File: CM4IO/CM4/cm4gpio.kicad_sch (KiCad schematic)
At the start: 2 parts

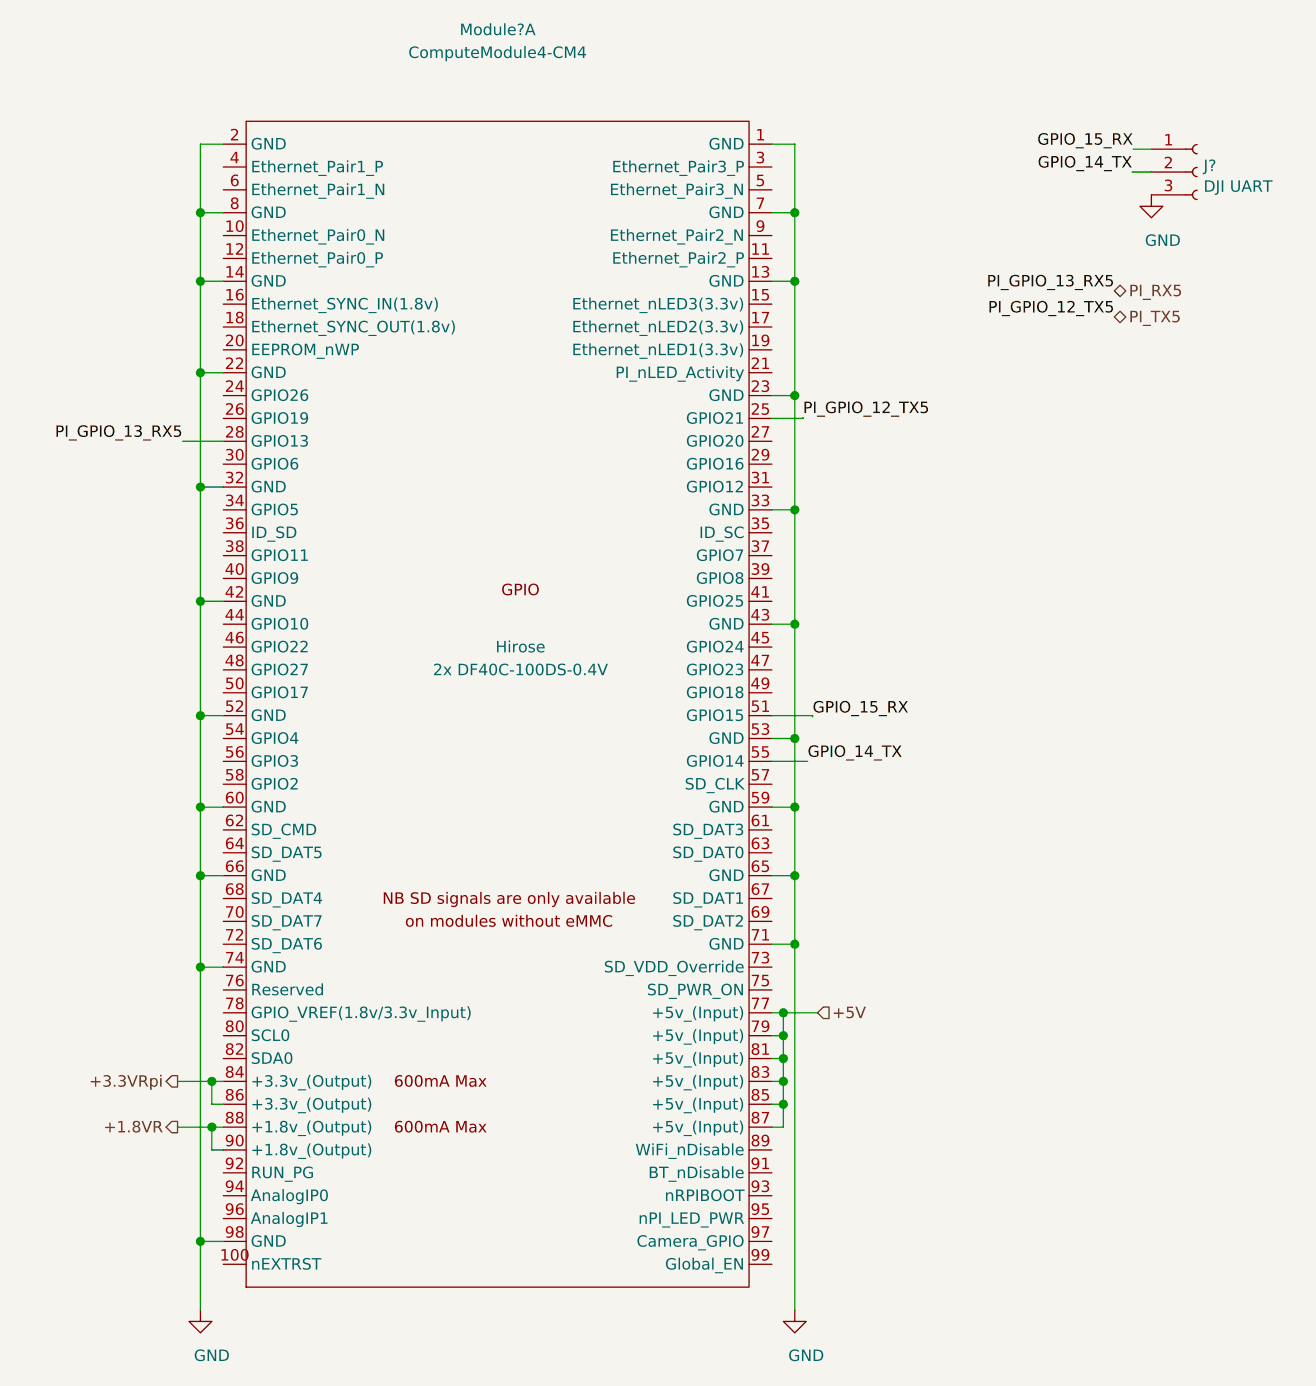
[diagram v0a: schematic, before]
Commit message: Initial CM4IO board design
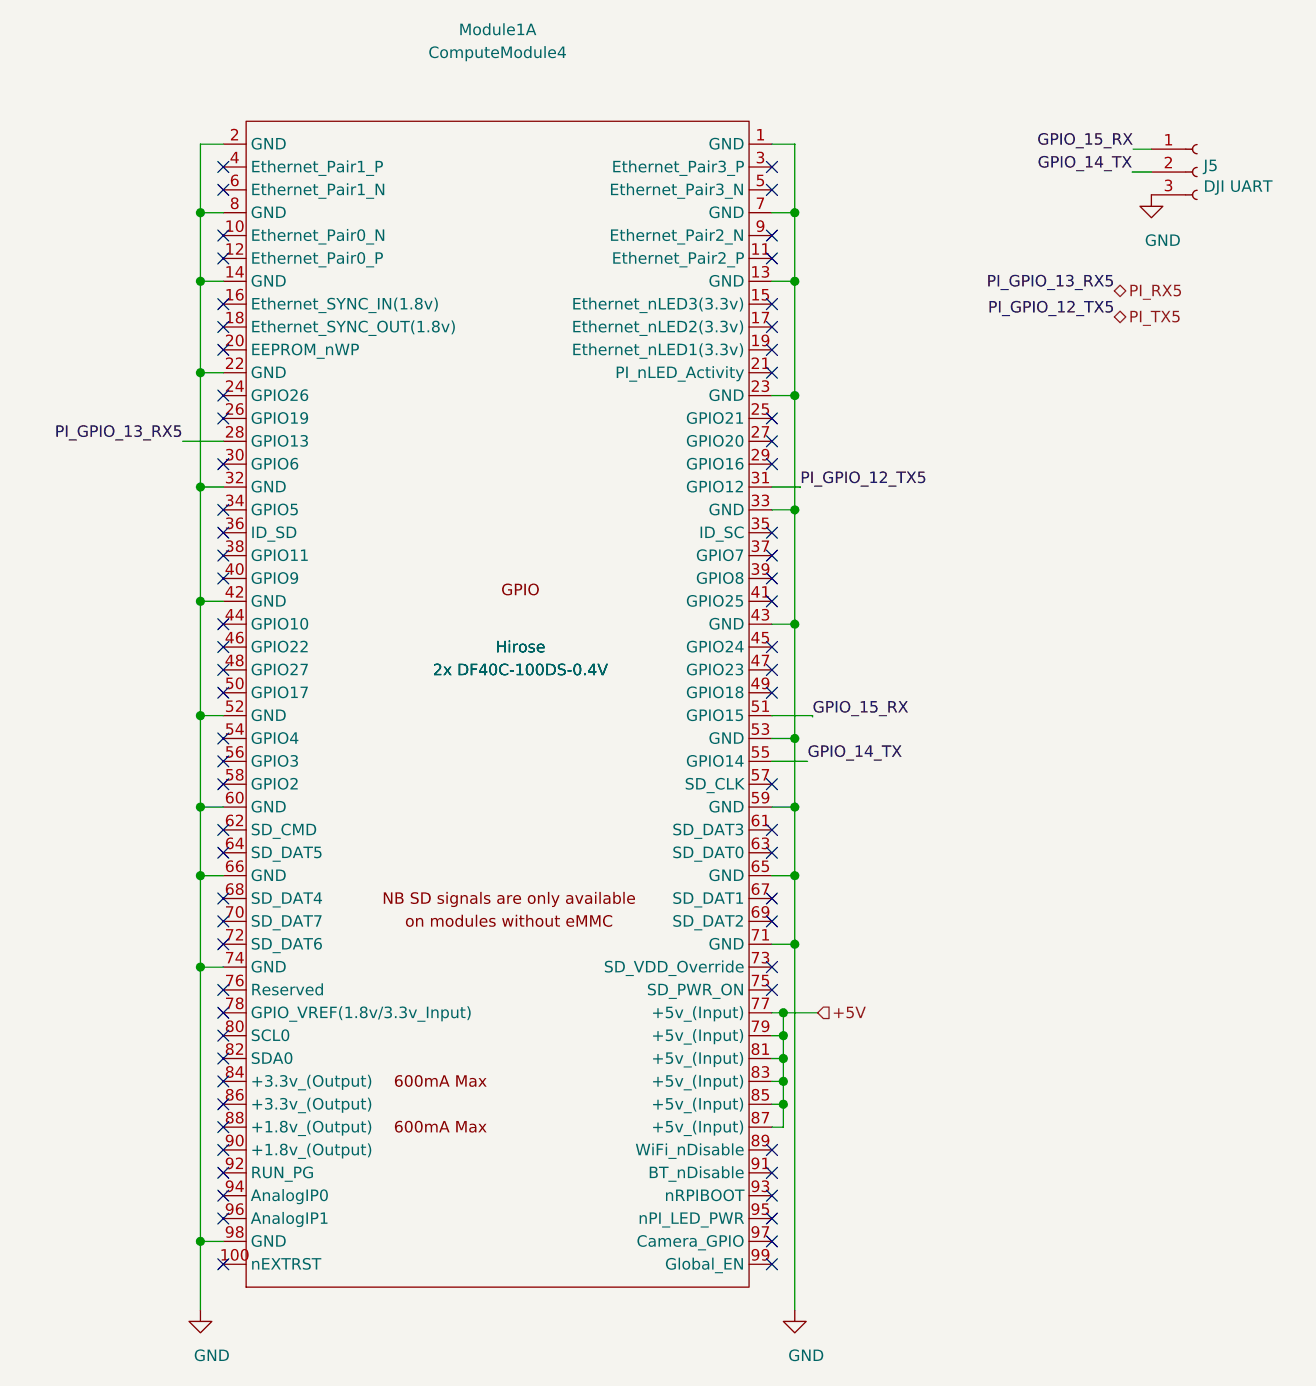
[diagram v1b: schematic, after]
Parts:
- J5: renamed from J?; footprint (none) -> Connector_Molex:Molex_PicoBlade_53261-0371_1x03-1MP_P1.25mm_Horizontal
- Module1: renamed from Module?; value ComputeModule4-CM4 -> ComputeModule4; Field4 (none) -> Hirose; Field5 (none) -> 2x DF40C-100DS-0.4V
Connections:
- net PI_TX5: now also Module1.31 (GPIO12); no longer Module1.25 (GPIO21)
- net +1.8VR: no longer names the net of Module1.88 (+1.8v_(Output))
- net +1.8VR: no longer Module1.90 (+1.8v_(Output))
- net +3.3VRpi: no longer names the net of Module1.84 (+3.3v_(Output))
- net +3.3VRpi: no longer Module1.86 (+3.3v_(Output))
- no-connect marks 0 -> 69
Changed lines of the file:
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@@
   (junction (at 61.8236 133.35) (diameter 1.016) (color 0 0 0 0))
   (junction (at 61.8236 163.83) (diameter 1.016) (color 0 0 0 0))
-  (junction (at 63.0936 146.05) (diameter 1.016) (color 0 0 0 0))
-  (junction (at 63.0936 151.13) (diameter 1.016) (color 0 0 0 0))
   (junction (at 126.5936 138.43) (diameter 1.016) (color 0 0 0 0))
   (junction (at 126.5936 140.97) (diameter 1.016) (color 0 0 0 0))
@@
   (junction (at 127.8636 123.19) (diameter 1.016) (color 0 0 0 0))
   (junction (at 127.8636 130.81) (diameter 1.016) (color 0 0 0 0))
-  (wire (pts (xy 59.2836 146.05) (xy 63.0936 146.05))
-    (stroke (width 0) (type solid) (color 0 0 0 0))
-  )
-  (wire (pts (xy 59.2836 151.13) (xy 63.0936 151.13))
-    (stroke (width 0) (type solid) (color 0 0 0 0))
-  )
+  (no_connect (at 64.3636 85.09))
+  (no_connect (at 125.3236 62.23))
+  (no_connect (at 125.3236 52.07))
+  (no_connect (at 125.3236 97.79))
+  (no_connect (at 64.3636 113.03))
+  (no_connect (at 125.3236 100.33))
+  (no_connect (at 125.3236 128.27))
+  (no_connect (at 64.3636 87.63))
+  (no_connect (at 125.3236 72.39))
+  (no_connect (at 125.3236 158.75))
+  (no_connect (at 64.3636 62.23))
+  (no_connect (at 64.3636 54.61))
+  (no_connect (at 64.3636 44.45))
+  (no_connect (at 64.3636 102.87))
+  (no_connect (at 64.3636 138.43))
+  (no_connect (at 125.3236 163.83))
+  (no_connect (at 125.3236 54.61))
+  (no_connect (at 125.3236 87.63))
+  (no_connect (at 125.3236 120.65))
+  (no_connect (at 64.3636 151.13))
+  (no_connect (at 125.3236 102.87))
+  (no_connect (at 64.3636 161.29))
+  (no_connect (at 64.3636 130.81))
+  (no_connect (at 125.3236 118.11))
+  (no_connect (at 64.3636 120.65))
+  (no_connect (at 64.3636 135.89))
+  (no_connect (at 125.3236 92.71))
+  (no_connect (at 64.3636 166.37))
+  (no_connect (at 64.3636 100.33))
+  (no_connect (at 64.3636 64.77))
+  (no_connect (at 125.3236 67.31))
+  (no_connect (at 125.3236 74.93))
+  (no_connect (at 64.3636 95.25))
+  (no_connect (at 64.3636 153.67))
+  (no_connect (at 125.3236 156.21))
+  (no_connect (at 125.3236 161.29))
+  (no_connect (at 64.3636 72.39))
+  (no_connect (at 64.3636 156.21))
+  (no_connect (at 64.3636 118.11))
+  (no_connect (at 125.3236 135.89))
+  (no_connect (at 64.3636 140.97))
+  (no_connect (at 125.3236 166.37))
+  (no_connect (at 64.3636 128.27))
+  (no_connect (at 64.3636 82.55))
+  (no_connect (at 125.3236 113.03))
+  (no_connect (at 64.3636 110.49))
+  (no_connect (at 64.3636 77.47))
+  (no_connect (at 64.3636 158.75))
+  (no_connect (at 64.3636 59.69))
+  (no_connect (at 125.3236 85.09))
+  (no_connect (at 125.3236 64.77))
+  (no_connect (at 125.3236 90.17))
+  (no_connect (at 125.3236 133.35))
+  (no_connect (at 125.3236 125.73))
+  (no_connect (at 64.3636 148.59))
+  (no_connect (at 64.3636 52.07))
+  (no_connect (at 64.3636 125.73))
+  (no_connect (at 64.3636 69.85))
+  (no_connect (at 125.3236 153.67))
+  (no_connect (at 64.3636 97.79))
+  (no_connect (at 125.3236 77.47))
+  (no_connect (at 64.3636 90.17))
+  (no_connect (at 64.3636 146.05))
+  (no_connect (at 125.3236 46.99))
+  (no_connect (at 64.3636 107.95))
+  (no_connect (at 64.3636 143.51))
+  (no_connect (at 64.3636 46.99))
+  (no_connect (at 125.3236 44.45))
+  (no_connect (at 125.3236 59.69))
   (wire (pts (xy 59.8424 74.93) (xy 64.3636 74.93))
     (stroke (width 0) (type solid) (color 0 0 0 0))
@@
     (stroke (width 0) (type solid) (color 0 0 0 0))
   )
-  (wire (pts (xy 63.0936 146.05) (xy 64.3636 146.05))
-    (stroke (width 0) (type solid) (color 0 0 0 0))
-  )
-  (wire (pts (xy 63.0936 148.59) (xy 63.0936 146.05))
-    (stroke (width 0) (type solid) (color 0 0 0 0))
-  )
-  (wire (pts (xy 63.0936 151.13) (xy 64.3636 151.13))
-    (stroke (width 0) (type solid) (color 0 0 0 0))
-  )
-  (wire (pts (xy 63.0936 153.67) (xy 63.0936 151.13))
-    (stroke (width 0) (type solid) (color 0 0 0 0))
-  )
   (wire (pts (xy 64.3636 41.91) (xy 61.8236 41.91))
     (stroke (width 0) (type solid) (color 0 0 0 0))
   )
-  (wire (pts (xy 64.3636 148.59) (xy 63.0936 148.59))
-    (stroke (width 0) (type solid) (color 0 0 0 0))
-  )
-  (wire (pts (xy 64.3636 153.67) (xy 63.0936 153.67))
-    (stroke (width 0) (type solid) (color 0 0 0 0))
-  )
   (wire (pts (xy 125.3236 41.91) (xy 127.8636 41.91))
     (stroke (width 0) (type solid) (color 0 0 0 0))
@@
     (stroke (width 0) (type solid) (color 0 0 0 0))
   )
-  (wire (pts (xy 125.3236 72.39) (xy 128.778 72.39))
+  (wire (pts (xy 125.3236 80.01) (xy 128.4732 80.01))
     (stroke (width 0) (type solid) (color 0 0 0 0))
   )
@@
     (stroke (width 0) (type solid) (color 0 0 0 0))
   )
-  (wire (pts (xy 128.778 72.39) (xy 128.778 72.2884))
+  (wire (pts (xy 128.4732 80.01) (xy 128.4732 80.0608))
     (stroke (width 0) (type solid) (color 0 0 0 0))
   )
@@
     (effects (font (size 1.27 1.27)) (justify right bottom))
   )
-  (label "PI_GPIO_12_TX5" (at 128.778 72.2884 0)
+  (label "PI_GPIO_12_TX5" (at 128.4732 80.0608 0)
     (effects (font (size 1.27 1.27)) (justify left bottom))
   )
@@
     (effects (font (size 1.27 1.27)) (justify right bottom))
   )
-  (hierarchical_label "+3.3VRpi" (shape output) (at 59.2836 146.05 180)
-    (effects (font (size 1.27 1.27)) (justify right))
-  )
-  (hierarchical_label "+1.8VR" (shape output) (at 59.2836 151.13 180)
-    (effects (font (size 1.27 1.27)) (justify right))
-  )
   (hierarchical_label "+5V" (shape input) (at 130.4036 138.43 0)
     (effects (font (size 1.27 1.27)) (justify left))
@@
   (symbol (lib_id "power:GND") (at 61.8236 171.45 0) (unit 1)
     (in_bom yes) (on_board yes)
-    (property "Reference" "#PWR?" (id 0) (at 61.8236 177.8 0)
+    (property "Reference" "#PWR069" (id 0) (at 61.8236 177.8 0)
       (effects (font (size 1.27 1.27)) hide)
     )
@@
   (symbol (lib_id "power:GND") (at 127.8636 171.45 0) (unit 1)
     (in_bom yes) (on_board yes)
-    (property "Reference" "#PWR?" (id 0) (at 127.8636 177.8 0)
+    (property "Reference" "#PWR070" (id 0) (at 127.8636 177.8 0)
       (effects (font (size 1.27 1.27)) hide)
     )
@@
   (symbol (lib_id "power:GND") (at 167.4876 47.5488 0) (unit 1)
     (in_bom yes) (on_board yes)
-    (property "Reference" "#PWR?" (id 0) (at 167.4876 53.8988 0)
+    (property "Reference" "#PWR068" (id 0) (at 167.4876 53.8988 0)
       (effects (font (size 1.27 1.27)) hide)
     )
@@
   (symbol (lib_id "Connector:Conn_01x03_Female") (at 172.5676 45.0088 0) (unit 1)
     (in_bom yes) (on_board yes)
-    (property "Reference" "J?" (id 0) (at 173.2789 44.3166 0)
+    (property "Reference" "J5" (id 0) (at 173.2789 44.3166 0)
       (effects (font (size 1.27 1.27)) (justify left))
     )
@@
       (effects (font (size 1.27 1.27)) (justify left))
     )
-    (property "Footprint" "" (id 2) (at 172.5676 45.0088 0)
+    (property "Footprint" "Connector_Molex:Molex_PicoBlade_53261-0371_1x03-1MP_P1.25mm_Horizontal" (id 2) (at 172.5676 45.0088 0)
       (effects (font (size 1.27 1.27)) hide)
     )
@@
   (symbol (lib_id "CM4IO:ComputeModule4-CM4") (at 97.3836 97.79 0) (unit 1)
     (in_bom yes) (on_board yes)
-    (property "Reference" "Module?" (id 0) (at 94.8436 29.21 0))
-    (property "Value" "ComputeModule4-CM4" (id 1) (at 94.8436 31.75 0))
-    (property "Footprint" "CM4IO:Raspberry-Pi-4-Compute-Module" (id 2) (at 239.6236 124.46 0)
+    (property "Reference" "Module1" (id 0) (at 94.844 29.21 0))
+    (property "Value" "ComputeModule4" (id 1) (at 94.844 31.75 0))
+    (property "Footprint" "CM4IO:Raspberry-Pi-4-Compute-Module" (id 2) (at 239.624 124.46 0)
       (effects (font (size 1.27 1.27)) hide)
     )
@@
       (effects (font (size 1.27 1.27)) hide)
     )
+    (property "Field4" "Hirose" (id 8) (at 97.3836 97.79 0))
+    (property "Field5" "2x DF40C-100DS-0.4V" (id 9) (at 97.3836 100.33 0))
   )
 )

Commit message: Completed H7/CM4IO Board
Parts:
- Module1: MPN 2x DF40C-100DS-0.4V -> (none); Manufacturer Hirose -> (none)
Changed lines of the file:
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@@
   (junction (at 127.8636 123.19) (diameter 1.016) (color 0 0 0 0))
   (junction (at 127.8636 130.81) (diameter 1.016) (color 0 0 0 0))
-  (no_connect (at 64.3636 85.09))
-  (no_connect (at 125.3236 62.23))
+  (no_connect (at 64.3636 153.67))
+  (no_connect (at 64.3636 118.11))
+  (no_connect (at 125.3236 153.67))
+  (no_connect (at 64.3636 151.13))
+  (no_connect (at 64.3636 59.69))
+  (no_connect (at 64.3636 161.29))
+  (no_connect (at 125.3236 113.03))
+  (no_connect (at 125.3236 135.89))
+  (no_connect (at 125.3236 156.21))
+  (no_connect (at 125.3236 128.27))
+  (no_connect (at 64.3636 64.77))
+  (no_connect (at 64.3636 69.85))
+  (no_connect (at 125.3236 54.61))
+  (no_connect (at 64.3636 52.07))
+  (no_connect (at 125.3236 161.29))
   (no_connect (at 125.3236 52.07))
-  (no_connect (at 125.3236 97.79))
-  (no_connect (at 64.3636 113.03))
-  (no_connect (at 125.3236 100.33))
-  (no_connect (at 125.3236 128.27))
-  (no_connect (at 64.3636 87.63))
-  (no_connect (at 125.3236 72.39))
-  (no_connect (at 125.3236 158.75))
-  (no_connect (at 64.3636 62.23))
-  (no_connect (at 64.3636 54.61))
-  (no_connect (at 64.3636 44.45))
-  (no_connect (at 64.3636 102.87))
-  (no_connect (at 64.3636 138.43))
-  (no_connect (at 125.3236 163.83))
-  (no_connect (at 125.3236 54.61))
-  (no_connect (at 125.3236 87.63))
-  (no_connect (at 125.3236 120.65))
-  (no_connect (at 64.3636 151.13))
+  (no_connect (at 64.3636 146.05))
+  (no_connect (at 64.3636 107.95))
   (no_connect (at 125.3236 102.87))
-  (no_connect (at 64.3636 161.29))
-  (no_connect (at 64.3636 130.81))
-  (no_connect (at 125.3236 118.11))
-  (no_connect (at 64.3636 120.65))
-  (no_connect (at 64.3636 135.89))
-  (no_connect (at 125.3236 92.71))
-  (no_connect (at 64.3636 166.37))
-  (no_connect (at 64.3636 100.33))
-  (no_connect (at 64.3636 64.77))
-  (no_connect (at 125.3236 67.31))
-  (no_connect (at 125.3236 74.93))
-  (no_connect (at 64.3636 95.25))
-  (no_connect (at 64.3636 153.67))
-  (no_connect (at 125.3236 156.21))
-  (no_connect (at 125.3236 161.29))
-  (no_connect (at 64.3636 72.39))
-  (no_connect (at 64.3636 156.21))
-  (no_connect (at 64.3636 118.11))
-  (no_connect (at 125.3236 135.89))
-  (no_connect (at 64.3636 140.97))
-  (no_connect (at 125.3236 166.37))
-  (no_connect (at 64.3636 128.27))
-  (no_connect (at 64.3636 82.55))
-  (no_connect (at 125.3236 113.03))
-  (no_connect (at 64.3636 110.49))
-  (no_connect (at 64.3636 77.47))
-  (no_connect (at 64.3636 158.75))
-  (no_connect (at 64.3636 59.69))
-  (no_connect (at 125.3236 85.09))
-  (no_connect (at 125.3236 64.77))
   (no_connect (at 125.3236 90.17))
   (no_connect (at 125.3236 133.35))
+  (no_connect (at 64.3636 140.97))
+  (no_connect (at 64.3636 85.09))
+  (no_connect (at 125.3236 77.47))
+  (no_connect (at 125.3236 166.37))
+  (no_connect (at 64.3636 166.37))
+  (no_connect (at 64.3636 120.65))
+  (no_connect (at 64.3636 138.43))
+  (no_connect (at 125.3236 67.31))
+  (no_connect (at 125.3236 100.33))
+  (no_connect (at 125.3236 120.65))
+  (no_connect (at 64.3636 143.51))
+  (no_connect (at 64.3636 62.23))
+  (no_connect (at 125.3236 44.45))
+  (no_connect (at 64.3636 95.25))
+  (no_connect (at 64.3636 82.55))
+  (no_connect (at 64.3636 113.03))
+  (no_connect (at 64.3636 148.59))
+  (no_connect (at 64.3636 158.75))
+  (no_connect (at 125.3236 62.23))
+  (no_connect (at 125.3236 72.39))
+  (no_connect (at 64.3636 100.33))
+  (no_connect (at 125.3236 163.83))
+  (no_connect (at 64.3636 128.27))
+  (no_connect (at 64.3636 130.81))
+  (no_connect (at 64.3636 54.61))
+  (no_connect (at 64.3636 110.49))
+  (no_connect (at 125.3236 87.63))
+  (no_connect (at 64.3636 87.63))
   (no_connect (at 125.3236 125.73))
-  (no_connect (at 64.3636 148.59))
-  (no_connect (at 64.3636 52.07))
+  (no_connect (at 125.3236 74.93))
+  (no_connect (at 64.3636 90.17))
+  (no_connect (at 125.3236 59.69))
   (no_connect (at 64.3636 125.73))
-  (no_connect (at 64.3636 69.85))
-  (no_connect (at 125.3236 153.67))
+  (no_connect (at 64.3636 72.39))
+  (no_connect (at 64.3636 44.45))
+  (no_connect (at 64.3636 156.21))
+  (no_connect (at 125.3236 92.71))
+  (no_connect (at 64.3636 102.87))
+  (no_connect (at 125.3236 64.77))
+  (no_connect (at 125.3236 158.75))
   (no_connect (at 64.3636 97.79))
-  (no_connect (at 125.3236 77.47))
-  (no_connect (at 64.3636 90.17))
-  (no_connect (at 64.3636 146.05))
+  (no_connect (at 125.3236 118.11))
   (no_connect (at 125.3236 46.99))
-  (no_connect (at 64.3636 107.95))
-  (no_connect (at 64.3636 143.51))
+  (no_connect (at 64.3636 77.47))
+  (no_connect (at 125.3236 97.79))
   (no_connect (at 64.3636 46.99))
-  (no_connect (at 125.3236 44.45))
-  (no_connect (at 125.3236 59.69))
+  (no_connect (at 125.3236 85.09))
+  (no_connect (at 64.3636 135.89))
   (wire (pts (xy 59.8424 74.93) (xy 64.3636 74.93))
     (stroke (width 0) (type solid) (color 0 0 0 0))
@@
       (effects (font (size 1.27 1.27)) hide)
     )
-    (property "Manufacturer" "Hirose" (id 8) (at 97.3836 97.79 0))
-    (property "MPN" "2x DF40C-100DS-0.4V" (id 9) (at 97.3836 100.33 0))
+    (property "Field4" "Hirose" (id 4) (at 97.3836 97.79 0))
+    (property "Field5" "2x DF40C-100DS-0.4V" (id 5) (at 97.3836 100.33 0))
     (property "Digi-Key_PN" "2x H11615CT-ND" (id 6) (at 97.3836 97.79 0)
       (effects (font (size 1.27 1.27)) hide)
@@
       (effects (font (size 1.27 1.27)) hide)
     )
-    (property "Field4" "Hirose" (id 8) (at 97.3836 97.79 0))
-    (property "Field5" "2x DF40C-100DS-0.4V" (id 9) (at 97.3836 100.33 0))
   )
 )
